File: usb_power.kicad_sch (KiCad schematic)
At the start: 0 parts

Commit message: Added usb block - still need to check
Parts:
- added C1, C133, C135, C2, C3: CL10A106KP8NNNC, easyeda2kicad:C0603, symbol easyeda2kicad:CL10A106KP8NNNC
- added C134: CL10A225KO8NNNC, easyeda2kicad:C0603, symbol easyeda2kicad:CL10A225KO8NNNC
- added C4: CL10A226MP8NUNE, easyeda2kicad:C0603, symbol easyeda2kicad:CL10A226MP8NUNE
- added D1, D3: 0603 Green 509-620mcd, easyeda2kicad:LED0603-RD, symbol easyeda2kicad:0603Green509-620mcd
- added D4: KT-0603R, easyeda2kicad:LED0603-RD, symbol easyeda2kicad:KT-0603R
- added D5: MBRA210LT3G_C5337989, easyeda2kicad:SMA_L4.3-W2.6-LS5.1-RD, symbol easyeda2kicad:MBRA210LT3G_C5337989
- added D6, D7, D8, D9: 0603ESDA-05N, easyeda2kicad:D0603-BI, symbol easyeda2kicad:0603ESDA-05N
- added J3: B2B-PH-SM4-TB (LF)(SN), easyeda2kicad:CONN-SMD_B2B-PH-SM4-TB-LF-SN, symbol easyeda2kicad:B2B-PH-SM4-TB(LF)(SN)
- added L1: FTC252012S1R0MBCA, easyeda2kicad:IND-SMD_L2.5-W2.0-VLS252012CX-150M, symbol easyeda2kicad:FTC252012S1R0MBCA
- added P1: TYPE-C 16PIN 2MD(073), easyeda2kicad:USB-C-SMD_TYPE-C-6PIN-2MD-073, symbol easyeda2kicad:TYPE-C16PIN2MD(073)
- added Q1: DMG2301L-7, easyeda2kicad:SOT-23-3_L2.9-W1.3-P1.90-LS2.4-BR, symbol easyeda2kicad:DMG2301L-7
- added R1: 0603WAF8060T5E, easyeda2kicad:R0603, symbol easyeda2kicad:0603WAF8060T5E
- added R10: 0603WAF1003T5E, easyeda2kicad:R0603, symbol easyeda2kicad:0603WAF1003T5E
- added R13: 0603WAF910JT5E, easyeda2kicad:R0603, symbol easyeda2kicad:0603WAF910JT5E
- added R15, R16, R7: 0603WAF5101T5E, easyeda2kicad:R0603, symbol easyeda2kicad:0603WAF5101T5E
- added R2, R5, R6: 0603WAF3300T5E, easyeda2kicad:R0603, symbol easyeda2kicad:0603WAF3300T5E
- added R3: 0603WAF7502T5E, easyeda2kicad:R0603, symbol easyeda2kicad:0603WAF7502T5E
- added R4: 0603WAF1431T5E, easyeda2kicad:R0603, symbol easyeda2kicad:0603WAF1431T5E
- added R8, R9: 0603WAF1002T5E, easyeda2kicad:R0603, symbol easyeda2kicad:0603WAF1002T5E
- added SW1: JS102011JCQN, easyeda2kicad:SW-SMD_JS102011JCQN, symbol easyeda2kicad:JS102011JCQN
- added TH1: NCP18XH103F03RB, easyeda2kicad:R0603, symbol easyeda2kicad:NCP18XH103F03RB
- added U2: MCP73833T-AMI/MF, easyeda2kicad:DFN-10_L3.0-W3.0-P0.50-BL-EP-1, symbol easyeda2kicad:MCP73833T-AMI_MF
- added U3: TPS631000DRLR, easyeda2kicad:SOT-583-8_L2.1-W1.2-P0.50-LS1.6-BL, symbol easyeda2kicad:TPS631000DRLR
- added U5: XC6206P332MR_C347376, easyeda2kicad:SOT-23-3_L3.0-W1.7-P0.95-LS2.9-BR, symbol easyeda2kicad:XC6206P332MR_C347376
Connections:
- new net: D3.2 (A), R5.1
- new net: R1.1, R13.2, U3.8 (FB)
- new net: D1.2 (A), R2.1
- new net: R8.1, R9.2
- new net: R3.2, R4.2, TH1.1
- new net: L1.2, U3.2 (LX2)
- new net: L1.1, U3.3 (LX1)
- new net: D4.2 (A), R6.1
- new net: R4.1, U2.8 (THERM)
- new net: R16.2, U2.6 (PROG)
- new net +3V3: C135.2, U5.2 (VOUT)
- new net +5V: C1.2, C133.2, C134.2, R1.2, U3.1 (VOUT), U5.3 (VIN)
- new net +5VP: C3.2, D5.2 (A), D6.2, D7.2, P1.11 (VBUS), P1.2 (VBUS), Q1.1 (G), R10.2, R5.2, R6.2, U2.1 (VDD), U2.2 (VDD)
- new net CC1: P1.4 (CC1), R7.2
- new net CC2: P1.10 (CC2), R15.2
- new net GND: C1.1, C133.1, C134.1, C135.1, C2.1, C3.1, C4.1, D1.1 (K), D6.1, D7.1, D8.1, D9.1, J3.2, P1.1 (GND), P1.12 (GND), P1.13 (SHELL), P1.14 (SHELL), R10.1, R13.1, R15.1, R16.1, R3.1, R7.1, R9.1, TH1.2, U2.11 (EP), U2.5 (VSS), U3.7 (GND), U5.1 (VSS)
- new net LIPO+: C4.2, J3.1, Q1.2 (S), R8.2, U2.10 (VBAT), U2.9 (VBAT)
- new net P_MODE: U3.6 (MODE)
- new net STAT1: D4.1 (K), U2.3 (STAT1)
- new net STAT2: D3.1 (K), U2.4 (STAT2)
- new net USB_D+: D9.2, P1.6 (DP1), P1.8 (DP2)
- new net USB_D-: D8.2, P1.5 (DN2), P1.7 (DN1)
- new net VIN: C2.2, R2.2, SW1.3, U3.4 (VIN), U3.5 (EN)
- new net raw_voltage: D5.1 (C), Q1.3 (D), SW1.2
- no-connect marks 0 -> 6
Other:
- note added: "'0' = switch is closed current flows rdson , no usb , board is powerd with the Lipo battery '1' = switch is open no current , battery is charging , usb will power board throught the schotkey diode"
- note added: "5V"
- note added: "BATT measurement voltage/2"
- note added: "Battery Connection and switch"
- note added: "Charger"
- note added: "Charging via USB C"
- note added: "I could replace this switch with a 2 pos"
- note added: "MCU Power"
- note added: "P FET and the schottky diode allows for simuntanioulous charge and circuit power"
- note added: "Pulldown for gate drive"
- note added: "Signals to MCU indicating state of charge"
- note added: "boost converter , 1cell lipo (3v to 4.2v) to 5v"

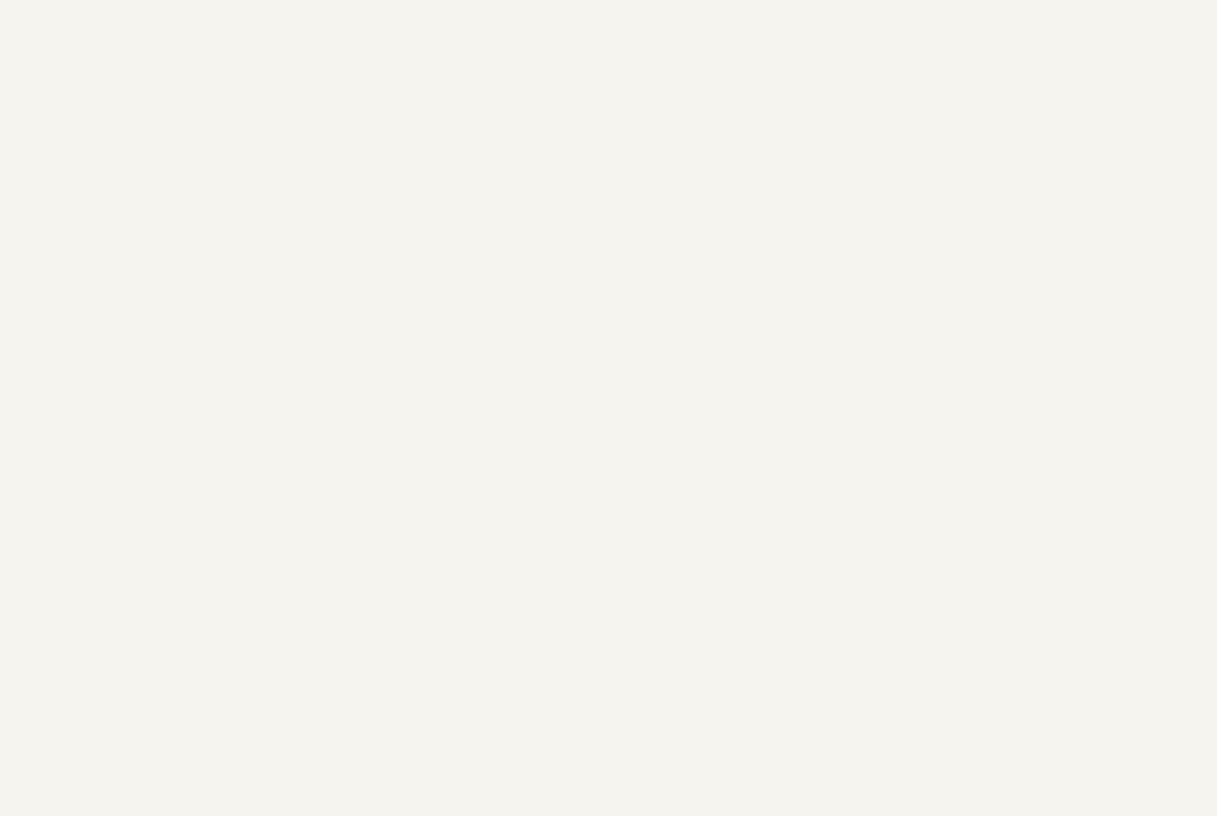
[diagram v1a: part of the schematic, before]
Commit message: Added some sensors and ch340
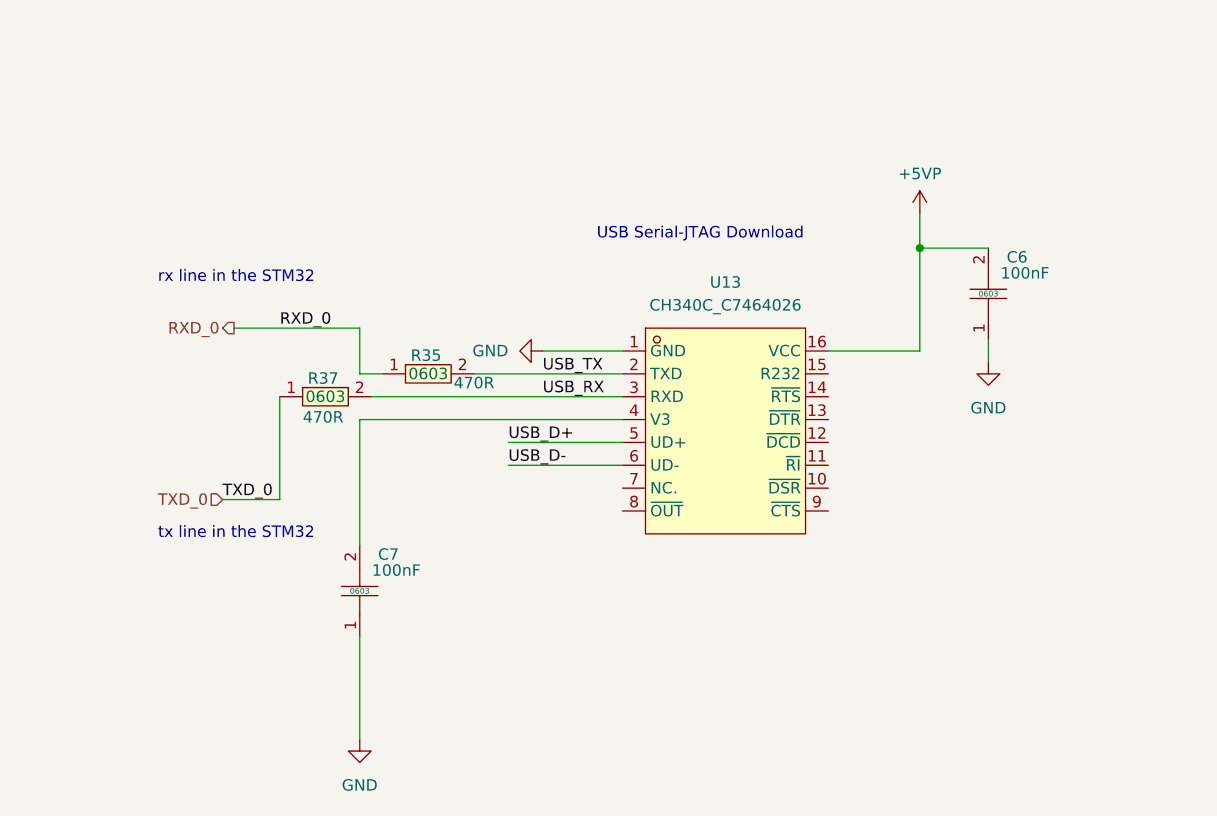
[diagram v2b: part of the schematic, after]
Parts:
- added C6, C7: CC0603KRX7R9BB104, easyeda2kicad:C0603, symbol easyeda2kicad:CC0603KRX7R9BB104
- added R35, R37: 0603WAF4700T5E, easyeda2kicad:R0603, symbol easyeda2kicad:0603WAF4700T5E
- added U13: CH340C_C7464026, easyeda2kicad:SOP-16_L10.0-W3.9-P1.27-LS6.0-BL, symbol easyeda2kicad:CH340C_C7464026
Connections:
- net +5VP: now also C6.2, U13.16 (VCC)
- net GND: now also C6.1, C7.1, U13.1 (GND)
- net USB_D+: now also U13.5 (UD+)
- net USB_D-: now also U13.6 (UD-)
- new net: C7.2, U13.4 (V3)
- new net RXD_0: R35.1
- new net TXD_0: R37.1
- new net USB_RX: R37.2, U13.3 (RXD)
- new net USB_TX: R35.2, U13.2 (TXD)
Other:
- note added: "USB Serial-JTAG Download"
- note added: "rx line in the STM32"
- note added: "tx line in the STM32"

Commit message: Added some sensors and current sensor
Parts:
- added R14, R17: 0603WAF1002T5E, easyeda2kicad:R0603, symbol easyeda2kicad:0603WAF1002T5E
- added U6: INA260AIPWR, easyeda2kicad:TSSOP-16_L5.0-W4.4-P0.65-LS6.4-BL-1, symbol easyeda2kicad:INA260AIPWR
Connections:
- net +3V3: now also R14.2, R17.2
- net +5V: now also U6.1 (IN+), U6.10 (VS), U6.12 (VBUS), U6.2 (IN+), U6.3 (IN+); no longer U5.3 (VIN)
- net GND: now also J3.1, U6.11 (GND), U6.4 (A1), U6.5 (A0), U6.6 (GND); no longer J3.2
- net LIPO+: now also J3.2; no longer J3.1
- new net: U5.3 (VIN), U6.14 (IN-), U6.15 (IN-), U6.16 (IN-)
- new net scl2: R14.1, U6.9 (SCL)
- new net sda2: R17.1, U6.8 (SDA)
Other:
- note added: "Address i2c = 0x40"

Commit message: Added led matrix and ina260
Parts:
- added CN1: SM04B-SRSS-TB (LF)(SN), easyeda2kicad:CONN-SMD_4P-P1.00_SM04B-SRSS-TB-LF-SN, symbol easyeda2kicad:SM04B-SRSS-TB(LF)(SN)
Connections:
- net +3V3: now also CN1.2
- net GND: now also CN1.1
- net scl2: now also CN1.4
- net sda2: now also CN1.3
